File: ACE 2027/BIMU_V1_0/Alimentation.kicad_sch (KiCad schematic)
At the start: 14 parts, among them U101 AP7361C-33E

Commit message: avancement
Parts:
- added J101: Conn_02x05_Odd_Even, Connector_Molex:Molex_Micro-Fit_3.0_43045-1000_2x05_P3.00mm_Horizontal, symbol Connector_Generic:Conn_02x05_Odd_Even
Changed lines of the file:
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@@
 		(dnp no)
 		(fields_autoplaced yes)
-		(property "Reference" "H102"
+		(property "Reference" "H?"
 			(at 223.52 29.2099 0)
 			(effects
@@
 				(path "/abeb93ed-b9ef-4503-99a7-3fce380ff294/6937e765-eead-4ea7-ba07-6590a34338ab"
 					(reference "H102")
+					(unit 1)
+				)
+			)
+			(project "Alimentation"
+				(path "/b9f9d5f5-b6f7-4b30-b419-fb6d3da99e85"
+					(reference "H?")
 					(unit 1)
 				)
@@
 	)
 	(symbol
+		(lib_id "Connector_Generic:Conn_02x05_Odd_Even")
+		(at 255.27 69.85 0)
+		(unit 1)
+		(exclude_from_sim no)
+		(in_bom yes)
+		(on_board yes)
+		(dnp no)
+		(fields_autoplaced yes)
+		(property "Reference" "J101"
+			(at 256.54 58.42 0)
+			(effects
+				(font
+					(size 1.27 1.27)
+				)
+			)
+		)
+		(property "Value" "Conn_02x05_Odd_Even"
+			(at 256.54 60.96 0)
+			(effects
+				(font
+					(size 1.27 1.27)
+				)
+			)
+		)
+		(property "Footprint" "Connector_Molex:Molex_Micro-Fit_3.0_43045-1000_2x05_P3.00mm_Horizontal"
+			(at 255.27 69.85 0)
+			(effects
+				(font
+					(size 1.27 1.27)
+				)
+				(hide yes)
+			)
+		)
+		(property "Datasheet" "~"
+			(at 255.27 69.85 0)
+			(effects
+				(font
+					(size 1.27 1.27)
+				)
+				(hide yes)
+			)
+		)
+		(property "Description" "Generic connector, double row, 02x05, odd/even pin numbering scheme (row 1 odd numbers, row 2 even numbers), script generated (kicad-library-utils/schlib/autogen/connector/)"
+			(at 255.27 69.85 0)
+			(effects
+				(font
+					(size 1.27 1.27)
+				)
+				(hide yes)
+			)
+		)
+		(pin "7"
+		)
+		(pin "1"
+		)
+		(pin "10"
+		)
+		(pin "2"
+		)
+		(pin "3"
+		)
+		(pin "5"
+		)
+		(pin "6"
+		)
+		(pin "8"
+		)
+		(pin "4"
+		)
+		(pin "9"
+		)
+		(instances
+			(project ""
+				(path "/b9f9d5f5-b6f7-4b30-b419-fb6d3da99e85"
+					(reference "J101")
+					(unit 1)
+				)
+			)
+		)
+	)
+	(symbol
 		(lib_id "power:+5V")
 		(at 34.29 33.02 0)
@@
 		(dnp no)
 		(fields_autoplaced yes)
-		(property "Reference" "H101"
+		(property "Reference" "H?"
 			(at 223.52 19.0499 0)
 			(effects
@@
 					(unit 1)
 				)
+			)
+			(project "Alimentation"
+				(path "/b9f9d5f5-b6f7-4b30-b419-fb6d3da99e85"
+					(reference "H?")
+					(unit 1)
+				)

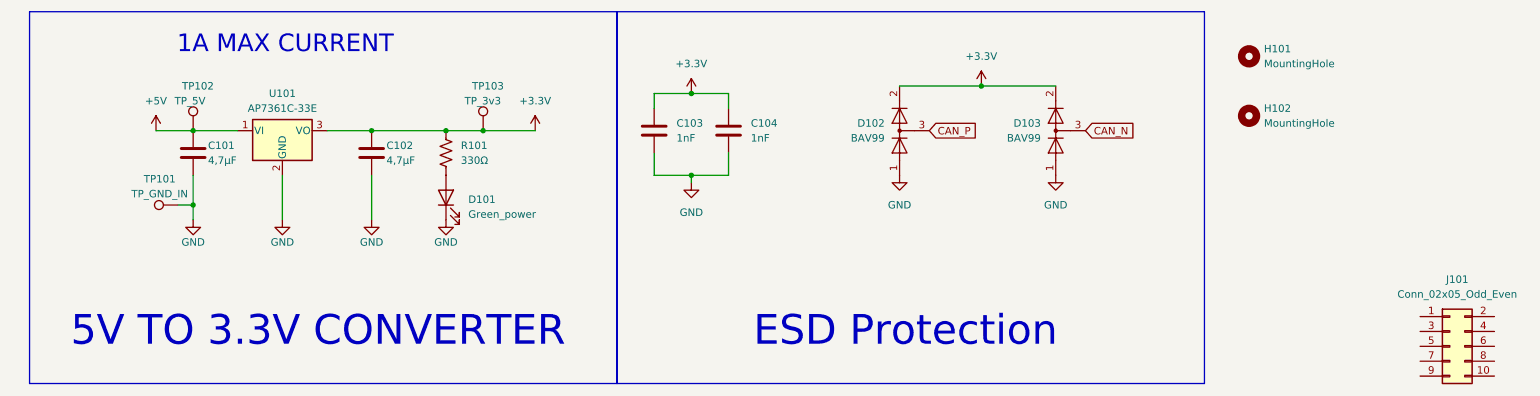
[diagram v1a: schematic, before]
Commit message: finalisation des connexions pour le BIMU. Il reste encore une révision à faire
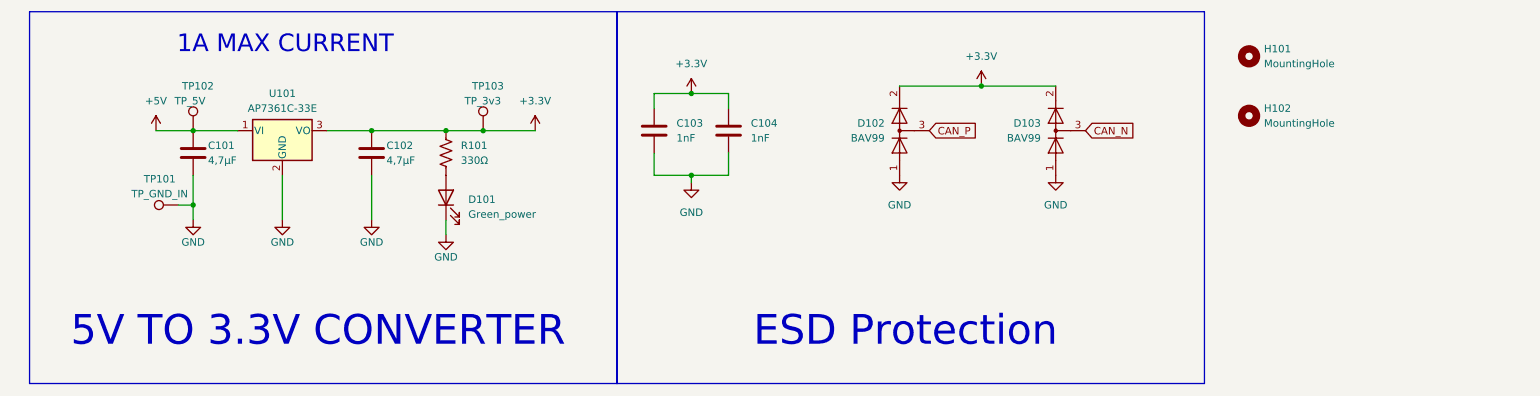
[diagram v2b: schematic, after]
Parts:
- removed J101: Conn_02x05_Odd_Even, Connector_Molex:Molex_Micro-Fit_3.0_43045-1000_2x05_P3.00mm_Horizontal, symbol Connector_Generic:Conn_02x05_Odd_Even
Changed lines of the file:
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@@
+	(wire
+		(pts
+			(xy 83.82 50.8) (xy 83.82 48.26)
+		)
+		(stroke
+			(width 0)
+			(type default)
+		)
+	)
 	(wire
 		(pts
@@
 		(dnp no)
 		(fields_autoplaced yes)
-		(property "Reference" "H?"
+		(property "Reference" "H102"
 			(at 223.52 29.2099 0)
 			(effects
@@
 	)
 	(symbol
-		(lib_id "Connector_Generic:Conn_02x05_Odd_Even")
-		(at 255.27 69.85 0)
-		(unit 1)
-		(exclude_from_sim no)
-		(in_bom yes)
-		(on_board yes)
-		(dnp no)
-		(fields_autoplaced yes)
-		(property "Reference" "J101"
-			(at 256.54 58.42 0)
-			(effects
-				(font
-					(size 1.27 1.27)
-				)
-			)
-		)
-		(property "Value" "Conn_02x05_Odd_Even"
-			(at 256.54 60.96 0)
-			(effects
-				(font
-					(size 1.27 1.27)
-				)
-			)
-		)
-		(property "Footprint" "Connector_Molex:Molex_Micro-Fit_3.0_43045-1000_2x05_P3.00mm_Horizontal"
-			(at 255.27 69.85 0)
-			(effects
-				(font
-					(size 1.27 1.27)
-				)
-				(hide yes)
-			)
-		)
-		(property "Datasheet" "~"
-			(at 255.27 69.85 0)
-			(effects
-				(font
-					(size 1.27 1.27)
-				)
-				(hide yes)
-			)
-		)
-		(property "Description" "Generic connector, double row, 02x05, odd/even pin numbering scheme (row 1 odd numbers, row 2 even numbers), script generated (kicad-library-utils/schlib/autogen/connector/)"
-			(at 255.27 69.85 0)
-			(effects
-				(font
-					(size 1.27 1.27)
-				)
-				(hide yes)
-			)
-		)
-		(pin "7"
-		)
-		(pin "1"
-		)
-		(pin "10"
-		)
-		(pin "2"
-		)
-		(pin "3"
-		)
-		(pin "5"
-		)
-		(pin "6"
-		)
-		(pin "8"
-		)
-		(pin "4"
-		)
-		(pin "9"
-		)
-		(instances
-			(project ""
-				(path "/b9f9d5f5-b6f7-4b30-b419-fb6d3da99e85"
-					(reference "J101")
-					(unit 1)
-				)
-			)
-		)
-	)
-	(symbol
 		(lib_id "power:+5V")
 		(at 34.29 33.02 0)
@@
 	(symbol
 		(lib_id "power:GND")
-		(at 83.82 48.26 0)
+		(at 83.82 50.8 0)
 		(unit 1)
 		(exclude_from_sim no)
@@
 		(dnp no)
 		(property "Reference" "#PWR0105"
+			(at 83.82 57.15 0)
+			(effects
+				(font
+					(size 1.27 1.27)
+				)
+				(hide yes)
+			)
+		)
+		(property "Value" "GND"
 			(at 83.82 54.61 0)
 			(effects
@@
 					(size 1.27 1.27)
 				)
-				(hide yes)
-			)
-		)
-		(property "Value" "GND"
-			(at 83.82 52.07 0)
-			(effects
-				(font
-					(size 1.27 1.27)
-				)
 			)
 		)
 		(property "Footprint" ""
-			(at 83.82 48.26 0)
+			(at 83.82 50.8 0)
 			(effects
 				(font
@@
 		)
 		(property "Datasheet" ""
-			(at 83.82 48.26 0)
+			(at 83.82 50.8 0)
 			(effects
 				(font
@@
 		)
 		(property "Description" "Power symbol creates a global label with name \"GND\" , ground"
-			(at 83.82 48.26 0)
+			(at 83.82 50.8 0)
 			(effects
 				(font
@@
 		(dnp no)
 		(fields_autoplaced yes)
-		(property "Reference" "H?"
+		(property "Reference" "H101"
 			(at 223.52 19.0499 0)
 			(effects

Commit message: Finalisé la révision du schéma
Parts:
- C101, C102: Digi-Key_PN (none) -> 1276-2970-1-ND
- C103, C104: Digi-Key_PN (none) -> 399-C1812C104MDRACTUCT-ND
- D101: value Green_power -> POWER LED; Digi-Key_PN (none) -> 1516-QBLP631-IG5CT-ND
- D102, D103: Digi-Key_PN (none) -> 1655-BAV99CT-ND
- H101, H102, TP101, TP102, TP103: now not fitted
- R101: Digi-Key_PN (none) -> 541-4168-1-ND
- U101: Digi-Key_PN (none) -> AP7361C-33E-13DICT-ND
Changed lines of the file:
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@@
 		(in_bom no)
 		(on_board yes)
-		(dnp no)
+		(dnp yes)
 		(fields_autoplaced yes)
 		(property "Reference" "H102"
@@
 			)
 		)
+		(property "Digi-Key_PN" "399-C1812C104MDRACTUCT-ND"
+			(at 119.38 33.02 0)
+			(effects
+				(font
+					(size 1.27 1.27)
+				)
+				(hide yes)
+			)
+		)
 		(pin "2"
 		)
@@
 			)
 		)
+		(property "Digi-Key_PN" "1655-BAV99CT-ND"
+			(at 187.96 33.02 90)
+			(effects
+				(font
+					(size 1.27 1.27)
+				)
+				(hide yes)
+			)
+		)
 		(pin "3"
 		)
@@
 			)
 		)
+		(property "Digi-Key_PN" "AP7361C-33E-13DICT-ND"
+			(at 55.88 33.02 0)
+			(effects
+				(font
+					(size 1.27 1.27)
+				)
+				(hide yes)
+			)
+		)
 		(pin "3"
 		)
@@
 			)
 		)
+		(property "Digi-Key_PN" "1276-2970-1-ND"
+			(at 71.12 36.83 0)
+			(effects
+				(font
+					(size 1.27 1.27)
+				)
+				(hide yes)
+			)
+		)
 		(pin "1"
 		)
@@
 		(in_bom yes)
 		(on_board yes)
-		(dnp no)
+		(dnp yes)
 		(property "Reference" "TP101"
 			(at 34.925 41.275 90)
@@
 			)
 		)
+		(property "Digi-Key_PN" "1655-BAV99CT-ND"
+			(at 161.29 33.02 90)
+			(effects
+				(font
+					(size 1.27 1.27)
+				)
+				(hide yes)
+			)
+		)
 		(pin "2"
 		)
@@
 			)
 		)
+		(property "Digi-Key_PN" "541-4168-1-ND"
+			(at 83.82 36.83 0)
+			(effects
+				(font
+					(size 1.27 1.27)
+				)
+				(hide yes)
+			)
+		)
 		(pin "2"
 		)
@@
 		(in_bom no)
 		(on_board yes)
-		(dnp no)
+		(dnp yes)
 		(fields_autoplaced yes)
 		(property "Reference" "H101"
@@
 			)
 		)
+		(property "Digi-Key_PN" "399-C1812C104MDRACTUCT-ND"
+			(at 132.08 33.02 0)
+			(effects
+				(font
+					(size 1.27 1.27)
+				)
+				(hide yes)
+			)
+		)
 		(pin "2"
 		)
@@
 		(in_bom yes)
 		(on_board yes)
-		(dnp no)
+		(dnp yes)
 		(property "Reference" "TP103"
 			(at 88.265 25.4 0)
@@
 			)
 		)
-		(property "Value" "Green_power"
+		(property "Value" "POWER LED"
 			(at 87.63 47.3074 90)
 			(effects
@@
 			)
 		)
+		(property "Digi-Key_PN" "1516-QBLP631-IG5CT-ND"
+			(at 83.82 44.45 90)
+			(effects
+				(font
+					(size 1.27 1.27)
+				)
+				(hide yes)
+			)
+		)
 		(pin "2"
 		)
@@
 		(in_bom yes)
 		(on_board yes)
-		(dnp no)
+		(dnp yes)
 		(property "Reference" "TP102"
 			(at 38.735 25.4 0)
@@
 			(at 40.64 36.83 0)
 			(effects
+				(font
+					(size 1.27 1.27)
+				)
+				(hide yes)
+			)
+		)
+		(property "Digi-Key_PN" "1276-2970-1-ND"
+			(at 40.64 36.83 0)
+			(effects

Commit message: Réglé les problèmes soulevé par la pull request
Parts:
- D101: footprint Diode_SMD:D_0805_2012Metric -> LED_SMD:LED_0805_2012Metric_Pad1.15x1.40mm_HandSolder
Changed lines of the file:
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@@
 	)
 	(symbol
+		(lib_name "LED_1")
 		(lib_id "Device:LED")
 		(at 83.82 44.45 90)
@@
 			)
 		)
-		(property "Footprint" "Diode_SMD:D_0805_2012Metric"
+		(property "Footprint" "LED_SMD:LED_0805_2012Metric_Pad1.15x1.40mm_HandSolder"
 			(at 83.82 44.45 0)
 			(effects
@@
 			)
 		)
+		(property "Sim.Pins" "1=K 2=A"
+			(at 83.82 44.45 0)
+			(effects
+				(font
+					(size 1.27 1.27)
+				)
+				(hide yes)
+			)
+		)
 		(property "Digi-Key_PN" "1516-QBLP631-IG5CT-ND"
 			(at 83.82 44.45 90)
@@
 		)
 		(instances
-			(project "BIMU_V_1"
+			(project ""
 				(path "/abeb93ed-b9ef-4503-99a7-3fce380ff294/6937e765-eead-4ea7-ba07-6590a34338ab"
 					(reference "D101")
 					(unit 1)
-				)
-			)
-			(project "Alimentation"
-				(path "/b9f9d5f5-b6f7-4b30-b419-fb6d3da99e85"
-					(reference "D101")
-					(unit 1)
